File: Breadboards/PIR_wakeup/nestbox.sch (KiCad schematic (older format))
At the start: 13 parts, among them P1 PINOUT, U1 MAX9061

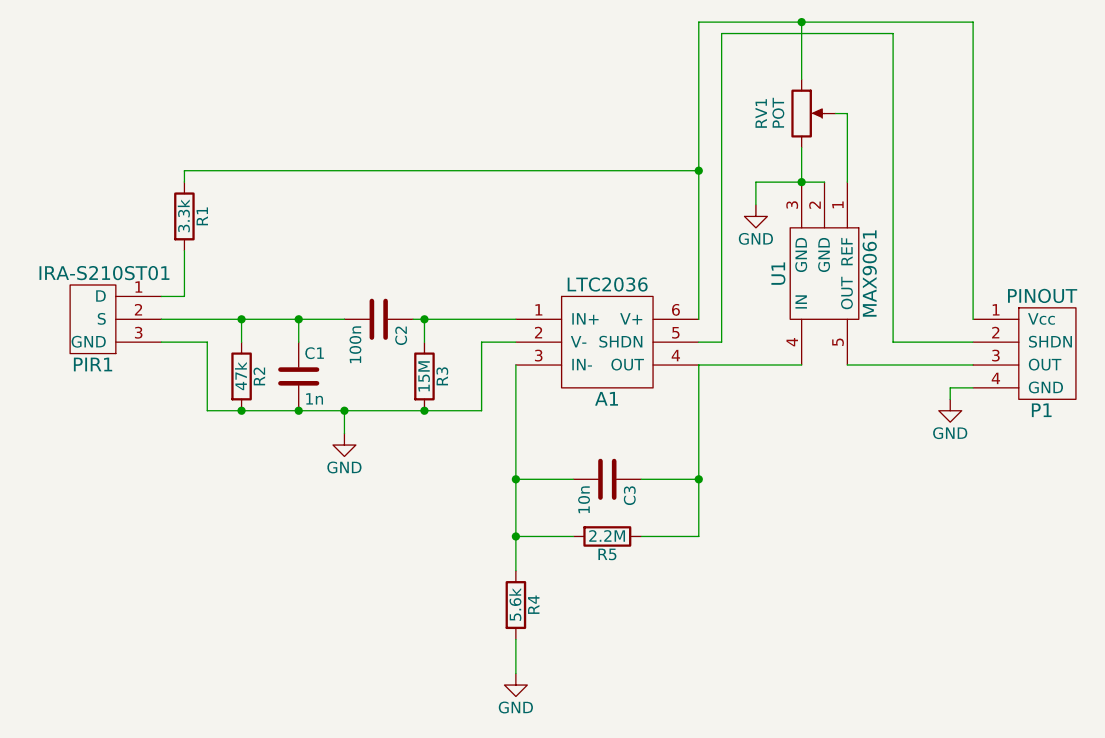
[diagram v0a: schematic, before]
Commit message: Updated version of PCB
-Added component values on silk
- Added output pin connections on silk
- Cleaned silk and made it consistent trough all components
- Changed vias width to comply to manufacturer specifications
- Added missing trace
- Added decoupling capacitor on power input
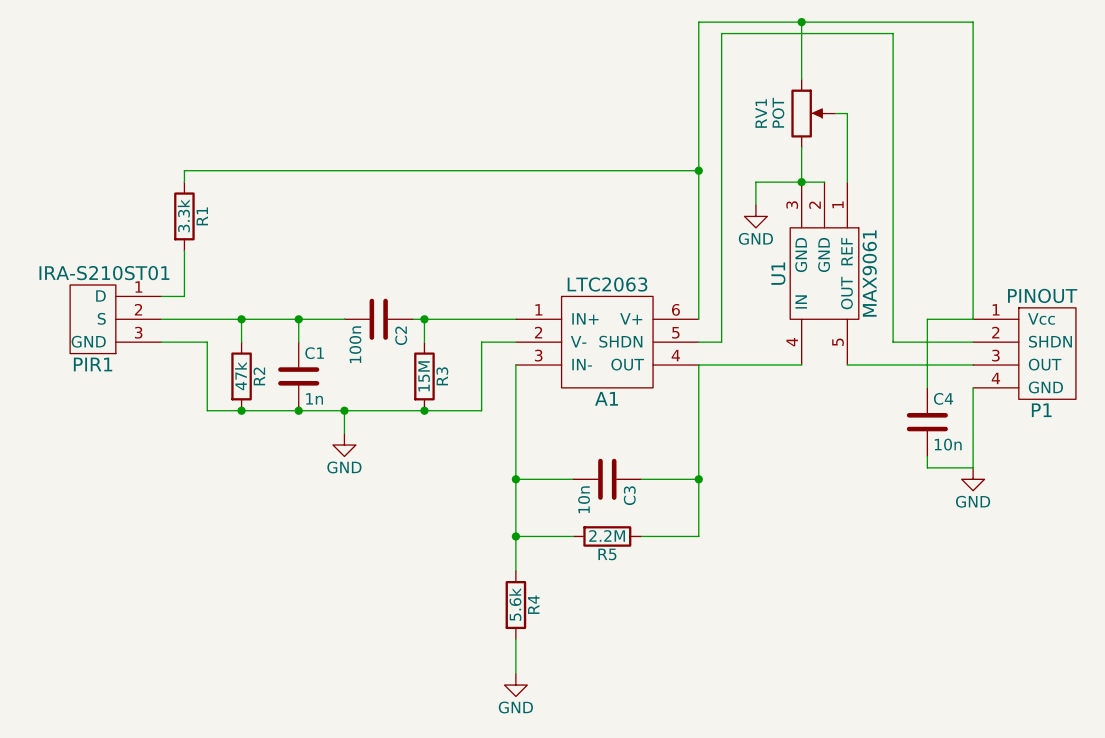
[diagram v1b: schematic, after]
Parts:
- added C4: 10n, Capacitors_SMD:C_0603_HandSoldering, symbol C
- A1: value LTC2036 -> LTC2063
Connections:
- net GND: now also C4.2
- net at A1.6 (V+), P1.1 (Vcc), R1.1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: now also C4.1
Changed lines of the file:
@@
 EESchema Schematic File Version 2
-LIBS:nestbox-rescue
 LIBS:power
 LIBS:device
@@
 P 6250 3800
 F 0 "A1" H 6250 3550 60  0000 C CNN
-F 1 "LTC2036" H 6250 4050 60  0000 C CNN
+F 1 "LTC2063" H 6250 4050 60  0000 C CNN
 F 2 "LTC:LTC2063" H 6250 4050 60  0001 C CNN
 F 3 "" H 6250 4050 60  0001 C CNN
@@
 Wire Wire Line
 	6750 3800 6650 3800
-$Comp
-L GND #PWR04
-U 1 1 5AF45304
-P 7750 4050
-F 0 "#PWR04" H 7750 3800 50  0001 C CNN
-F 1 "GND" H 7750 3900 50  0000 C CNN
-F 2 "" H 7750 4050 50  0001 C CNN
-F 3 "" H 7750 4050 50  0001 C CNN
-	1    7750 4050
-	1    0    0    -1
-$EndComp
-Wire Wire Line
-	7850 4000 7750 4000
-Wire Wire Line
-	7750 4000 7750 4050
 Wire Wire Line
 	7850 3700 7850 2400
@@
 Wire Wire Line
 	4300 3600 4400 3600
+$Comp
+L C C4
+U 1 1 5AF829F5
+P 7650 4150
+F 0 "C4" H 7675 4250 50  0000 L CNN
+F 1 "10n" H 7675 4050 50  0000 L CNN
+F 2 "Capacitors_SMD:C_0603_HandSoldering" H 7688 4000 50  0001 C CNN
+F 3 "" H 7650 4150 50  0001 C CNN
+	1    7650 4150
+	1    0    0    -1
+$EndComp
+Wire Wire Line
+	7850 4000 7850 4350
+Wire Wire Line
+	7850 4350 7650 4350
+Wire Wire Line
+	7650 4350 7650 4300
+Wire Wire Line
+	7650 4000 7650 3700
+Wire Wire Line
+	7650 3700 7850 3700
+$Comp
+L GND #PWR04
+U 1 1 5AF82B3A
+P 7850 4350
+F 0 "#PWR04" H 7850 4100 50  0001 C CNN
+F 1 "GND" H 7850 4200 50  0000 C CNN
+F 2 "" H 7850 4350 50  0001 C CNN
+F 3 "" H 7850 4350 50  0001 C CNN
+	1    7850 4350
+	1    0    0    -1
+$EndComp
 $EndSCHEMATC
